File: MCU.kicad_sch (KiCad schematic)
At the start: 24 parts, among them J1 USB_C_Receptacle_USB2.0, J2 Conn_01x05_Male, J5 Cortex_Debug, M4 Module-mega-mcu144-0.3, M5 Module-input-0.1, P10 Pad, P11 Pad, P12 Pad, P13 Pad, P14 Pad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

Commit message: Fab preview
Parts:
- removed M5: Module-input-0.1, hellen-one-input-0.1:input, symbol hellen-one-input-0.1:Module-input-0.1
- removed R94, R95: 510k, hellen-one-common:R0603, symbol hellen-one-common:Res
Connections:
- net +5VA: no longer M4.N30 (V5A_SWITCHABLE)
- net CAM_PULLDOWN: now also M4.N20 (IO4); no longer M4.E22 (OUT_IO8)
- net D2_PULLDOWN: now also M4.E20 (OUT_IO13); no longer M4.N21 (IO3)
- net D3_PULLDOWN: now also M4.E22 (OUT_IO8); no longer M4.N20 (IO4)
- net TACH: now also M4.N21 (IO3); no longer M4.E20 (OUT_IO13)
- net at P7.1 (Pin_1): now also M4.N13 (SPI3_MOSI); no longer M4.E3 (SPI2_MOSI)
- net at P5.1 (Pin_1): now also M4.N11 (SPI3_SCK); no longer M4.E1 (SPI2_SCK)
- net at M4.E2 (SPI2_MISO): no longer P6.1 (Pin_1)
- net at M4.E35 (IO6): no longer P14.1 (Pin_1)
- net at M4.E36 (IO7): no longer P15.1 (Pin_1)
- net at M4.E4 (SPI2_CS): no longer P8.1 (Pin_1)
- net at M4.N10 (SPI3_CS): now also P8.1 (Pin_1)
- net at M4.N12 (SPI3_MISO): now also P6.1 (Pin_1)
- net at M4.N24 (UART8_RX): now also P14.1 (Pin_1)
- net at M4.N25 (UART8_TX): now also P15.1 (Pin_1)
- net VREF: now reaches M4.S35 (VREF1)
- net VREF2: no longer names the net of M4.S5 (VREF2)
- no-connect marks 32 -> 21
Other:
- note removed: "Сделать без input"
- moved on the sheet: P14, P15, P5, P6, P7, P8

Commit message: Fab export
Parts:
- removed M4: Module-mega-mcu144-0.3, hellen-one-mega-mcu144-0.3:mega-mcu144, symbol mega-mcu144:Module-mega-mcu144-0.3
- added M4: Module-mega-mcu144-0.4, hellen-one-mega-mcu144-0.4:mega-mcu144, symbol hellen-one-mega-mcu144-0.4:Module-mega-mcu144-0.4
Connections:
- net +3.3V: now also M4.N22 (V33)
- net +3.3VA: now also M4.N28 (V33_SWITCHABLE)
- net +5V: now also M4.N31 (VCC)
- net +5VA: now also M4.E38 (V5A_SWITCHABLE), M4.W2 (V5A_SWITCHABLE)
- net 2STEP_PULLDOWN: now also M4.E23 (OUT_IO7)
- net AIN1: now also M4.S32 (IN_TPS2)
- net AIN2: now also M4.S33 (IN_PPS2)
- net AIN3: now also M4.S21 (IN_MAP1)
- net AIN4: now also M4.S11 (IN_AUX3)
- net CAM_PULLDOWN: now also M4.N20 (IO4)
- net CAM_VR_PULLUP: now also M4.E11 (OUT_IO9)
- net CAN+: now also M4.W12 (CANH)
- net CAN-: now also M4.W13 (CANL)
- net CRANK_N_PULLUP: now also M4.E7 (OUT_IO5)
- net CRANK_P_PULLUP: now also M4.E12 (OUT_IO2)
- net D2_PULLDOWN: now also M4.E20 (OUT_IO13)
- net D3_PULLDOWN: now also M4.E22 (OUT_IO8)
- net D4_PULLDOWN: now also M4.E33 (OUT_INJ7)
- net D5_PULLDOWN: now also M4.E34 (OUT_INJ8)
- net ETB_DIR: now also M4.N16 (IO1)
- net ETB_DIS: now also M4.N19 (IO2)
- net ETB_PWM: now also M4.E17 (OUT_PWM2)
- net GND: now also M4.G (GND)
- net GNDA: now also M4.E39 (GNDA), M4.W1 (GNDA)
- net HALL1: now also M4.S4 (IN_D1)
- net HALL2: now also M4.S2 (IN_D3)
- net HALL3: now also M4.S1 (IN_D4)
- net HS1: now also M4.E25 (OUT_PWM7)
- net HS2: now also M4.E28 (OUT_PWM8)
- net IN_2STEP: now also M4.S25 (IN_VSS)
- net IN_AFR: now also M4.S15 (IN_O2S2)
- net IN_CAM_HALL: now also M4.S24 (IN_CAM)
- net IN_CAM_VR: now also M4.S17 (IN_RES1)
- net IN_CLT: now also M4.S28 (IN_CLT)
- net IN_CRANK: now also M4.S22 (IN_CRANK)
- net IN_D2: now also M4.S9 (IN_SENS1)
- net IN_D3: now also M4.S8 (IN_SENS2)
- net IN_D4: now also M4.S7 (IN_SENS3)
- net IN_D5: now also M4.S6 (IN_SENS4)
- net IN_FLEX: now also M4.S10 (IN_AUX4)
- net IN_IAT: now also M4.S26 (IN_IAT)
- net IN_KNOCK: now also M4.S23 (IN_KNOCK)
- net IN_MAP: now also M4.S20 (IN_MAP2)
- net IN_MAP2: now also M4.S19 (IN_MAP3)
- net IN_PPS1: now also M4.S31 (IN_PPS)
- net IN_PPS2: now also M4.S12 (IN_AUX2)
- net IN_TPS1: now also M4.S30 (IN_TPS)
- net IN_TPS2: now also M4.S13 (IN_AUX1)
- net MAIN: now also M4.E10 (OUT_IO10)
- net MCU_BOOST: now also M4.E16 (OUT_PWM3)
- net MCU_FAN_RELAY: now also M4.E24 (OUT_IO11)
- net MCU_IDLE1: now also M4.E27 (OUT_PWM1)
- net MCU_IDLE2: now also M4.E14 (OUT_PWM5)
- net MCU_INJ1: now also M4.E19 (OUT_INJ1)
- net MCU_INJ2: now also M4.E18 (OUT_INJ2)
- net MCU_INJ3: now also M4.E29 (OUT_INJ3)
- net MCU_INJ4: now also M4.E30 (OUT_INJ4)
- net MCU_INJ5: now also M4.E31 (OUT_INJ5)
- net MCU_INJ6: now also M4.E32 (OUT_INJ6)
- net NOS: now also M4.E9 (OUT_IO6)
- net NRESET: now also M4.N9 (nReset)
- net OUT_IGN1: now also M4.W11 (IGN1)
- net OUT_IGN2: now also M4.W10 (IGN2)
- net OUT_IGN3: now also M4.W9 (IGN3)
- net OUT_IGN4: now also M4.W8 (IGN4)
- net OUT_IGN5: now also M4.W7 (IGN5)
- net OUT_IGN6: now also M4.W6 (IGN6)
- net PUMP_RELAY: now also M4.E13 (OUT_IO12)
- net PWR_EN: now also M4.N29 (OUT_PWR_EN)
- net SWCLK: now also M4.N8 (SWCLK)
- net SWDIO: now also M4.N7 (SWDIO)
- net SWO: now also M4.N6 (SWO)
- net TACH: now also M4.N21 (IO3)
- net TACH_PULLUP: now also M4.E8 (OUT_IO1)
- net TEMP_PULLUP: now also M4.E21 (OUT_IO4)
- net THRESHOLD_VR_CM: now also M4.E15 (OUT_PWM4)
- net THRESHOLD_VR_CR: now also M4.E26 (OUT_PWM6)
- net TLS115_PG: now also M4.S3 (IN_D2)
- net UART_RX: now also M4.N18 (UART2_RX)
- net UART_TX: now also M4.N17 (UART2_TX)
- net USB+: now also M4.N3 (USBP)
- net USB-: now also M4.N2 (USBM)
- net VBUS: now also M4.N4 (VBUS)
- net VIGN: now also M4.N26 (IN_VIGN)
- net VREF: now also M4.S35 (VREF1)
- net VR_ANALOG_CM: now also M4.S14 (IN_RES2)
- net VR_ANALOG_CR: now also M4.S18 (IN_RES3)
- net VVT1: now also M4.W5 (IGN7)
- net VVT2: now also M4.W4 (IGN8)
- net at P7.1 (Pin_1): now also M4.N13 (SPI3_MOSI)
- net at P5.1 (Pin_1): now also M4.N11 (SPI3_SCK)
- net at P9.1 (Pin_1): now also M4.S29 (IN_AT2)
- net at P10.1 (Pin_1): now also M4.E6 (OUT_IO3)
- net at P8.1 (Pin_1): now also M4.N10 (SPI3_CS)
- net at P6.1 (Pin_1): now also M4.N12 (SPI3_MISO)
- net at P13.1 (Pin_1): now also M4.N14 (I2C_SCL)
- net at P12.1 (Pin_1): now also M4.N15 (I2C_SDA)
- net at P14.1 (Pin_1): now also M4.N24 (UART8_RX)
- net at P15.1 (Pin_1): now also M4.N25 (UART8_TX)
- net at P11.1 (Pin_1): now also M4.S27 (IN_AT1)

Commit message: Export
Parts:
- removed J2: Conn_01x05_Male, Connector_Molex:Molex_SPOX_5267-05A_1x05_P2.50mm_Vertical, symbol Connector:Conn_01x05_Male
- removed M4: Module-mega-mcu144-0.4, hellen-one-mega-mcu144-0.4:mega-mcu144, symbol hellen-one-mega-mcu144-0.4:Module-mega-mcu144-0.4
- added J5: Conn_01x05_Male, Connector_Molex:Molex_SPOX_5267-05A_1x05_P2.50mm_Vertical, symbol Connector:Conn_01x05_Pin
- added M4: Module-mega-mcu144-0.5, hellen-one-mega-mcu144-0.5:mega-mcu144, symbol hellen-one-mega-mcu144-0.5:Module-mega-mcu144-0.5
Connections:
- net +3.3V: now also M4.N22 (V33)
- net +3.3VA: now also M4.N28 (V33_SWITCHABLE)
- net +5V: now also M4.N31 (VCC)
- net +5VA: now also M4.E38 (V5A_SWITCHABLE), M4.W2 (V5A_SWITCHABLE)
- net AIN1: now also M4.S32 (IN_TPS2)
- net AIN2: now also M4.S33 (IN_PPS2)
- net AIN3: now also M4.S21 (IN_MAP1)
- net AIN4: now also M4.S11 (IN_AUX3)
- net CAM_VR_PULLUP: now also M4.E11 (OUT_IO9)
- net CAN+: now also M4.W12 (CANH)
- net CAN-: now also M4.W13 (CANL)
- net CRANK_N_PULLUP: now also M4.E7 (OUT_IO5)
- net CRANK_P_PULLUP: now also M4.E12 (OUT_IO2)
- net D2_PULLDOWN: now also M4.E20 (OUT_IO13)
- net D3_PULLDOWN: now also M4.E22 (OUT_IO8)
- net D4_PULLDOWN: now also M4.E33 (OUT_INJ7)
- net D5_PULLDOWN: now also M4.E34 (OUT_INJ8)
- net ETB_DIR: now also M4.N16 (IO1)
- net ETB_DIS: now also M4.N19 (IO2)
- net ETB_PWM: now also M4.E17 (OUT_PWM2)
- net GND: now also J5.4 (Pin_4), J5.5 (Pin_5), M4.G (GND)
- net GNDA: now also M4.E39 (GNDA), M4.W1 (GNDA)
- net HALL1: now also M4.S4 (IN_D1)
- net HALL2: now also M4.S2 (IN_D3)
- net HALL3: now also M4.S1 (IN_D4)
- net HS1: now also M4.E25 (OUT_PWM7)
- net HS2: now also M4.E28 (OUT_PWM8)
- net IN_2STEP: now also M4.S25 (IN_VSS)
- net IN_AFR: now also M4.S15 (IN_O2S2)
- net IN_CAM_HALL: now also M4.S24 (IN_CAM)
- net IN_CAM_VR: now also M4.S17 (IN_RES1)
- net IN_CLT: now also M4.S28 (IN_CLT)
- net IN_CRANK: now also M4.S22 (IN_CRANK)
- net IN_D2: now also M4.S9 (IN_SENS1)
- net IN_D3: now also M4.S8 (IN_SENS2)
- net IN_D4: now also M4.S7 (IN_SENS3)
- net IN_D5: now also M4.S6 (IN_SENS4)
- net IN_FLEX: now also M4.S10 (IN_AUX4)
- net IN_IAT: now also M4.S26 (IN_IAT)
- net IN_KNOCK: now also M4.S23 (IN_KNOCK)
- net IN_MAP: now also M4.S20 (IN_MAP2)
- net IN_MAP2: now also M4.S19 (IN_MAP3)
- net IN_PPS1: now also M4.S31 (IN_PPS)
- net IN_PPS2: now also M4.S12 (IN_AUX2)
- net IN_TPS1: now also M4.S30 (IN_TPS)
- net IN_TPS2: now also M4.S13 (IN_AUX1)
- net MAIN: now also M4.E10 (OUT_IO10)
- net MCU_BOOST: now also M4.E16 (OUT_PWM3)
- net MCU_FAN_RELAY: now also M4.E24 (OUT_IO11)
- net MCU_IDLE1: now also M4.E27 (OUT_PWM1)
- net MCU_IDLE2: now also M4.E14 (OUT_PWM5)
- net MCU_INJ1: now also M4.E19 (OUT_INJ1)
- net MCU_INJ2: now also M4.E18 (OUT_INJ2)
- net MCU_INJ3: now also M4.E29 (OUT_INJ3)
- net MCU_INJ4: now also M4.E30 (OUT_INJ4)
- net MCU_INJ5: now also M4.E31 (OUT_INJ5)
- net MCU_INJ6: now also M4.E32 (OUT_INJ6)
- net NOS: now also M4.E9 (OUT_IO6)
- net NRESET: now also M4.N9 (nReset)
- net OUT_IGN1: now also M4.W11 (IGN1)
- net OUT_IGN2: now also M4.W10 (IGN2)
- net OUT_IGN3: now also M4.W9 (IGN3)
- net OUT_IGN4: now also M4.W8 (IGN4)
- net OUT_IGN5: now also M4.W7 (IGN5)
- net OUT_IGN6: now also M4.W6 (IGN6)
- net PUMP_RELAY: now also M4.E13 (OUT_IO12)
- net PWR_EN: now also M4.N29 (OUT_PWR_EN)
- net SWCLK: now also M4.N8 (SWCLK)
- net SWDIO: now also M4.N7 (SWDIO)
- net SWO: now also M4.N6 (SWO)
- net TACH: now also M4.N21 (IO3)
- net TACH_PULLUP: now also M4.E8 (OUT_IO1)
- net TEMP_PULLUP: now also M4.E21 (OUT_IO4)
- net THRESHOLD_VR_CM: now also M4.E15 (OUT_PWM4)
- net THRESHOLD_VR_CR: now also M4.E26 (OUT_PWM6)
- net TLS115_PG: now also M4.S3 (IN_D2)
- net UART_RX: now also M4.N18 (UART2_RX)
- net UART_TX: now also M4.N17 (UART2_TX)
- net USB+: now also J5.3 (Pin_3), M4.N3 (USBP)
- net USB-: now also J5.2 (Pin_2), M4.N2 (USBM)
- net VBUS: now also J5.1 (Pin_1), M4.N4 (VBUS)
- net VIGN: now also M4.N26 (IN_VIGN)
- net VREF: now also M4.S35 (VREF1)
- net VR_ANALOG_CM: now also M4.S14 (IN_RES2)
- net VR_ANALOG_CR: now also M4.S18 (IN_RES3)
- net VVT1: now also M4.W5 (IGN7)
- net VVT2: now also M4.W4 (IGN8)
- net at P7.1 (Pin_1): now also M4.N13 (SPI3_MOSI)
- net at P10.1 (Pin_1): now also M4.E6 (OUT_IO3)
- net at P8.1 (Pin_1): now also M4.N10 (SPI3_CS)
- net at P5.1 (Pin_1): now also M4.N11 (SPI3_SCK)
- net at P6.1 (Pin_1): now also M4.N12 (SPI3_MISO)
- net at P13.1 (Pin_1): now also M4.N14 (I2C_SCL)
- net at P12.1 (Pin_1): now also M4.N15 (I2C_SDA)
- net at P14.1 (Pin_1): now also M4.N24 (UART8_RX)
- net at P15.1 (Pin_1): now also M4.N25 (UART8_TX)
- net at P11.1 (Pin_1): now also M4.S27 (IN_AT1)
- net at P9.1 (Pin_1): now also M4.S29 (IN_AT2)
- new net 2STEP_PULLUP: M4.E23 (OUT_IO7)
- new net CAM_PULLUP: M4.N20 (IO4)
- new net IN_CAM2_VR: M4.E36 (IO7)
- no-connect marks 21 -> 20
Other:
- note removed: "Занулить резисторы HALL"

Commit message: Replace
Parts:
- U1: footprint alphax-2ch:JDY-33 -> kicad6-libraries:JDY-33
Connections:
- no-connect marks 20 -> 23
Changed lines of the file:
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@@
   (junction (at 207.01 173.99) (diameter 0) (color 0 0 0 0)
+  )
+  (junction (at 175.26 152.4) (diameter 0) (color 0 0 0 0)
   )
   (junction (at 261.62 130.81) (diameter 1.016) (color 0 0 0 0)
@@
   (no_connect (at 160.02 214.63))
   (no_connect (at 160.02 77.47))
+  (no_connect (at 181.61 147.32))
+  (no_connect (at 181.61 149.86))
   (no_connect (at 189.23 171.45))
-  (no_connect (at 181.61 138.43))
+  (no_connect (at 181.61 137.16))
   (no_connect (at 201.93 171.45))
-  (no_connect (at 181.61 140.97))
+  (no_connect (at 181.61 139.7))
+  (no_connect (at 181.61 143.51))
   (no_connect (at 160.02 176.53))
   (no_connect (at 97.79 293.37))
@@
     (stroke (width 0) (type default))
   )
-  (bus (pts (xy 175.26 151.13) (xy 175.26 156.21))
-    (stroke (width 0) (type default))
-  )
-  (wire (pts (xy 176.53 135.89) (xy 176.53 132.08))
+  (bus (pts (xy 175.26 151.13) (xy 175.26 152.4))
+    (stroke (width 0) (type default))
+  )
+  (wire (pts (xy 176.53 135.89) (xy 176.53 130.81))
     (stroke (width 0) (type default))
   )
@@
     (stroke (width 0) (type default))
   )
+  (bus (pts (xy 175.26 152.4) (xy 175.26 156.21))
+    (stroke (width 0) (type default))
+  )
   (wire (pts (xy 245.11 107.95) (xy 245.11 105.41))
     (stroke (width 0) (type default))
@@
     (stroke (width 0) (type default))
   )
-  (polyline (pts (xy 176.53 181.61) (xy 176.53 152.4))
+  (polyline (pts (xy 176.53 181.61) (xy 176.53 156.21))
     (stroke (width 0) (type dash))
   )
@@
     (stroke (width 0) (type default))
   )
-  (wire (pts (xy 181.61 132.08) (xy 176.53 132.08))
-    (stroke (width 0) (type default))
-  )
-  (bus (pts (xy 224.79 113.03) (xy 224.79 148.59))
-    (stroke (width 0) (type default))
-  )
-  (polyline (pts (xy 219.71 152.4) (xy 176.53 152.4))
+  (wire (pts (xy 181.61 130.81) (xy 176.53 130.81))
+    (stroke (width 0) (type default))
+  )
+  (bus (pts (xy 224.79 113.03) (xy 224.79 152.4))
+    (stroke (width 0) (type default))
+  )
+  (polyline (pts (xy 219.71 156.21) (xy 176.53 156.21))
     (stroke (width 0) (type dash))
   )
@@
     (stroke (width 0) (type solid))
   )
-  (wire (pts (xy 179.07 138.43) (xy 179.07 134.62))
+  (wire (pts (xy 179.07 138.43) (xy 179.07 133.35))
     (stroke (width 0) (type default))
   )
@@
     (stroke (width 0) (type default))
   )
+  (bus (pts (xy 175.26 152.4) (xy 224.79 152.4))
+    (stroke (width 0) (type default))
+  )
   (wire (pts (xy 207.01 166.37) (xy 207.01 168.91))
     (stroke (width 0) (type default))
   )
-  (polyline (pts (xy 219.71 181.61) (xy 219.71 152.4))
+  (polyline (pts (xy 219.71 181.61) (xy 219.71 156.21))
     (stroke (width 0) (type dash))
   )
@@
   )
   (wire (pts (xy 85.09 81.28) (xy 97.79 81.28))
-    (stroke (width 0) (type default))
-  )
-  (bus (pts (xy 224.79 148.59) (xy 175.26 148.59))
     (stroke (width 0) (type default))
   )
@@
     (stroke (width 0) (type default))
   )
-  (wire (pts (xy 179.07 134.62) (xy 181.61 134.62))
+  (wire (pts (xy 179.07 133.35) (xy 181.61 133.35))
     (stroke (width 0) (type default))
   )
@@
     (effects (font (size 1.27 1.27)) (justify right bottom))
   )
-  (text "MCU Debug Port" (at 217.4546 155.3723 0)
+  (text "MCU Debug Port" (at 217.17 160.02 0)
     (effects (font (size 1.27 1.27)) (justify right bottom))
   )
@@
     )
   )
-  (symbol (lib_id "JDY-33:JDY-33") (at 185.42 133.858 0) (unit 1)
-    (in_bom yes) (on_board yes) (dnp no)
-    (property "Reference" "U1" (at 204.47 132.08 0)
+  (symbol (lib_id "JDY-33:JDY-33") (at 185.42 133.35 0) (unit 1)
+    (in_bom yes) (on_board yes) (dnp no)
+    (property "Reference" "U1" (at 204.47 131.572 0)
       (effects (font (size 1.27 1.27)) (justify left))
     )
-    (property "Value" "JDY-33" (at 204.47 134.62 0)
+    (property "Value" "JDY-33" (at 204.47 134.112 0)
       (effects (font (size 1.27 1.27)) (justify left))
     )
-    (property "Footprint" "alphax-2ch:JDY-33" (at 185.42 133.858 0)
+    (property "Footprint" "kicad6-libraries:JDY-33" (at 185.42 133.35 0)
       (effects (font (size 1.27 1.27)) (justify left bottom) hide)
     )
-    (property "Datasheet" "https://datasheet.lcsc.com/lcsc/2106070033_QIACHIP-WL9981TC_C2689544.pdf" (at 185.42 133.858 0)
+    (property "Datasheet" "https://datasheet.lcsc.com/lcsc/2106070033_QIACHIP-WL9981TC_C2689544.pdf" (at 185.42 133.35 0)
       (effects (font (size 1.27 1.27)) (justify left bottom) hide)
     )
-    (property "LCSC" "" (at 185.42 133.858 0)
-      (effects (font (size 1.27 1.27)) hide)
-    )
-    (property "PARTREV" "v1.0" (at 185.42 133.858 0)
+    (property "LCSC" "" (at 185.42 133.35 0)
+      (effects (font (size 1.27 1.27)) hide)
+    )
+    (property "PARTREV" "v1.0" (at 185.42 133.35 0)
       (effects (font (size 1.27 1.27)) (justify left bottom) hide)
     )
-    (property "MF" "HuiCheng" (at 185.42 133.858 0)
+    (property "MF" "HuiCheng" (at 185.42 133.35 0)
       (effects (font (size 1.27 1.27)) (justify left bottom) hide)
     )
-    (property "STANDARD" "Manufacturer Recommendations" (at 185.42 133.858 0)
+    (property "STANDARD" "Manufacturer Recommendations" (at 185.42 133.35 0)
       (effects (font (size 1.27 1.27)) (justify left bottom) hide)
     )
@@
     (pin "5")
     (pin "6")
+    (pin "16")
+    (pin "17")
+    (pin "15")
     (instances
       (project "alphax_4ch"
@@
     )
   )
-  (symbol (lib_id "power:GND") (at 181.61 127 0) (unit 1)
-    (in_bom yes) (on_board yes) (dnp no)
-    (property "Reference" "#PWR079" (at 181.61 133.35 0)
-      (effects (font (size 1.27 1.27)) hide)
-    )
-    (property "Value" "GND" (at 181.61 130.81 0)
-      (effects (font (size 1.27 1.27)))
-    )
+  (symbol (lib_id "power:GND") (at 181.61 127 270) (unit 1)
+    (in_bom yes) (on_board yes) (dnp no)
+    (property "Reference" "#PWR079" (at 175.26 127 0)
+      (effects (font (size 1.27 1.27)) hide)
+    )
+    (property "Value" "GND" (at 177.8 127 0)
+      (effects (font (size 1.27 1.27)))
+    )

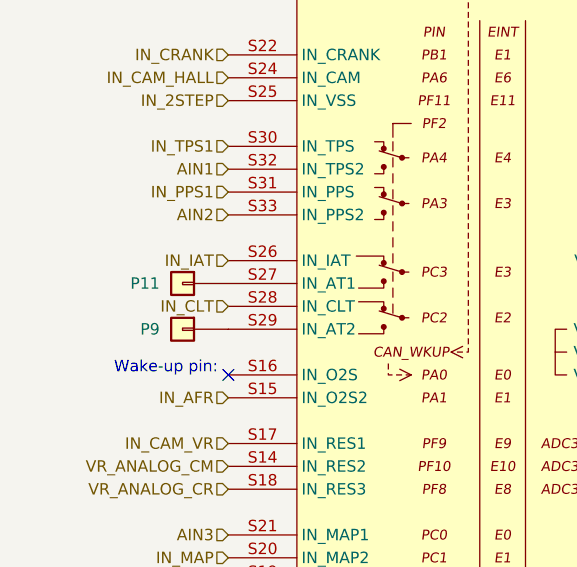
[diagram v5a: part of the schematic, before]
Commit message: Main relay voltage AT1
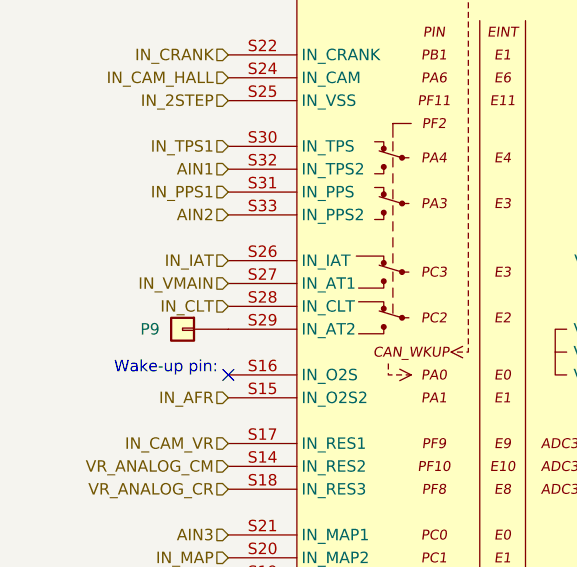
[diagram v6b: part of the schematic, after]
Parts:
- removed P11: Pad, hellen-one-common:PAD-TH, symbol hellen-one-common:Pad
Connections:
- net IN_VMAIN: now reaches M4.S27 (IN_AT1)
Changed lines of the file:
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@@
     (effects (font (size 1.27 1.27)) (justify left))
+  )
+  (hierarchical_label "IN_VMAIN" (shape input) (at 97.79 212.09 180) (fields_autoplaced)
+    (effects (font (size 1.27 1.27)) (justify right))
   )
   (hierarchical_label "2STEP_PULLUP" (shape output) (at 97.79 163.83 180) (fields_autoplaced)
@@
     (pin "12")
     (pin "13")
+    (pin "15")
+    (pin "16")
+    (pin "17")
     (pin "2")
     (pin "5")
     (pin "6")
-    (pin "16")
-    (pin "17")
-    (pin "15")
     (instances
       (project "alphax_4ch"
@@
         )
       )
-    )
-  )
-  (symbol (lib_id "hellen-one-common:Pad") (at 92.71 212.09 0) (mirror y) (unit 1)
-    (in_bom yes) (on_board yes) (dnp no) (fields_autoplaced)
-    (property "Reference" "P11" (at 90.17 212.0899 0)
-      (effects (font (size 1.27 1.27)) (justify left))
-    )
-    (property "Value" "Pad" (at 92.71 214.63 0)
-      (effects (font (size 1.27 1.27)) hide)
-    )
-    (property "Footprint" "hellen-one-common:PAD-TH" (at 92.71 215.9 0)
-      (effects (font (size 1.27 1.27)) hide)
-    )
-    (property "Datasheet" "~" (at 92.71 212.09 0)
-      (effects (font (size 1.27 1.27)) hide)
-    )
-    (pin "1")
-    (instances
-      (project "alphax_4ch"
-        (path "/63d2dd9f-d5ff-4811-a88d-0ba932475460"
-          (reference "P11") (unit 1)
-        )
-        (path "/63d2dd9f-d5ff-4811-a88d-0ba932475460/c3470145-cca5-462e-8136-3f6ead667763"
-          (reference "P20") (unit 1)
-        )
-      )
